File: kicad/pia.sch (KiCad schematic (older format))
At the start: 9 parts, among them J3 DB25_Male, U11 6821, U13 74HC04, U14 74LS245

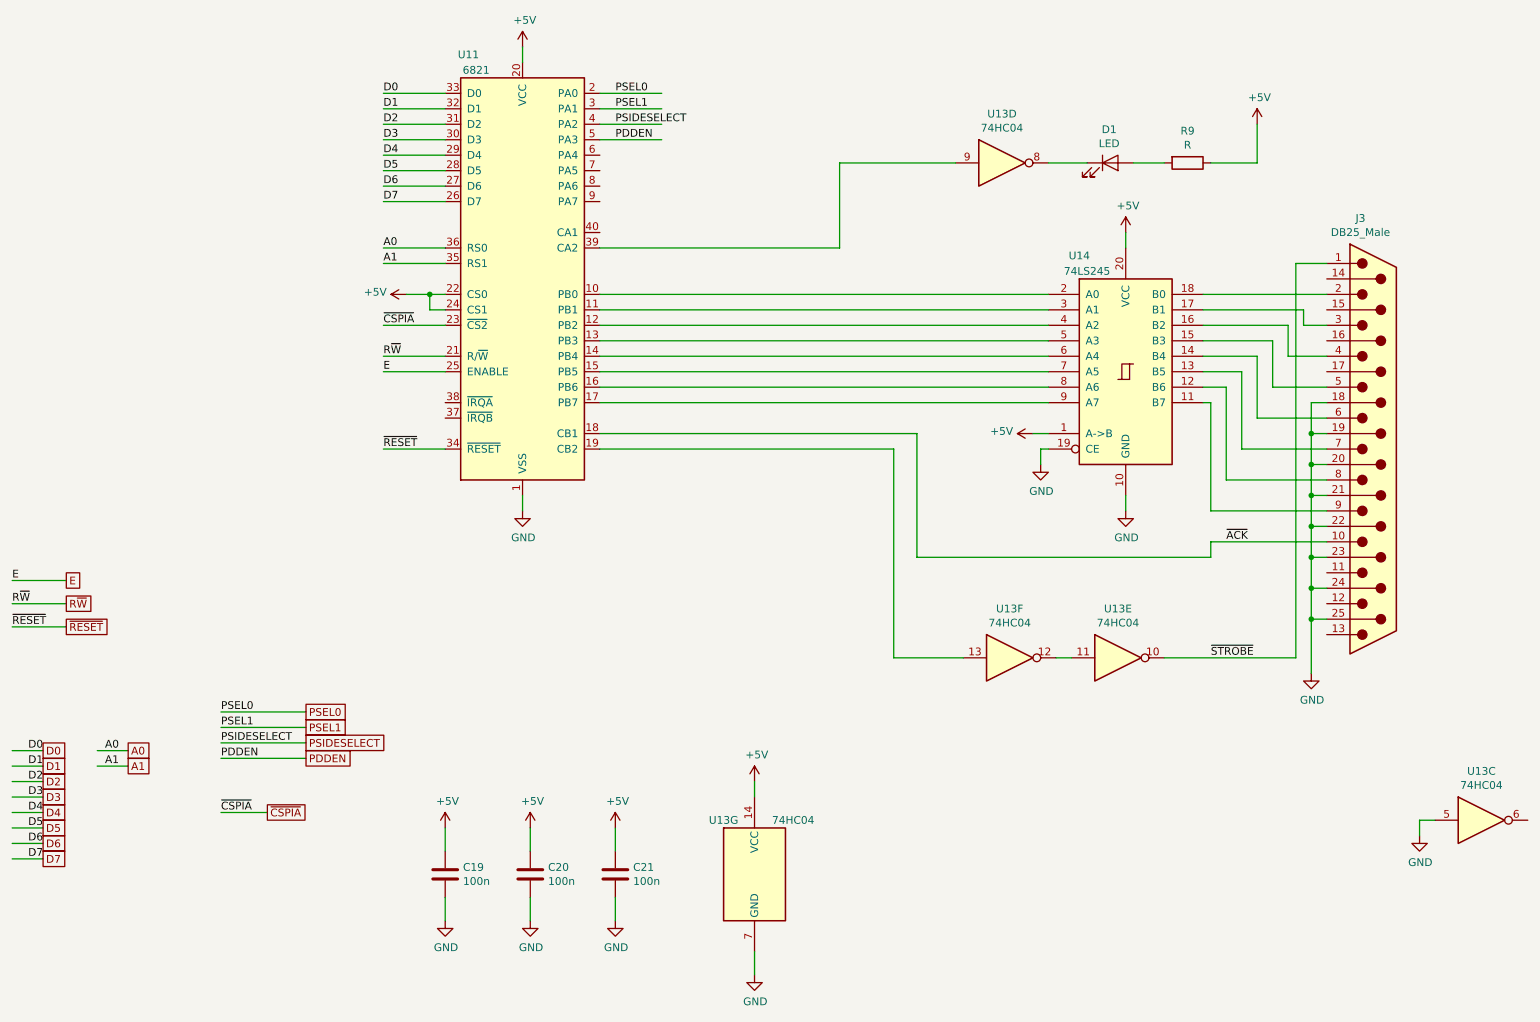
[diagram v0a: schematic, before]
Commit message: Adding PCB layout
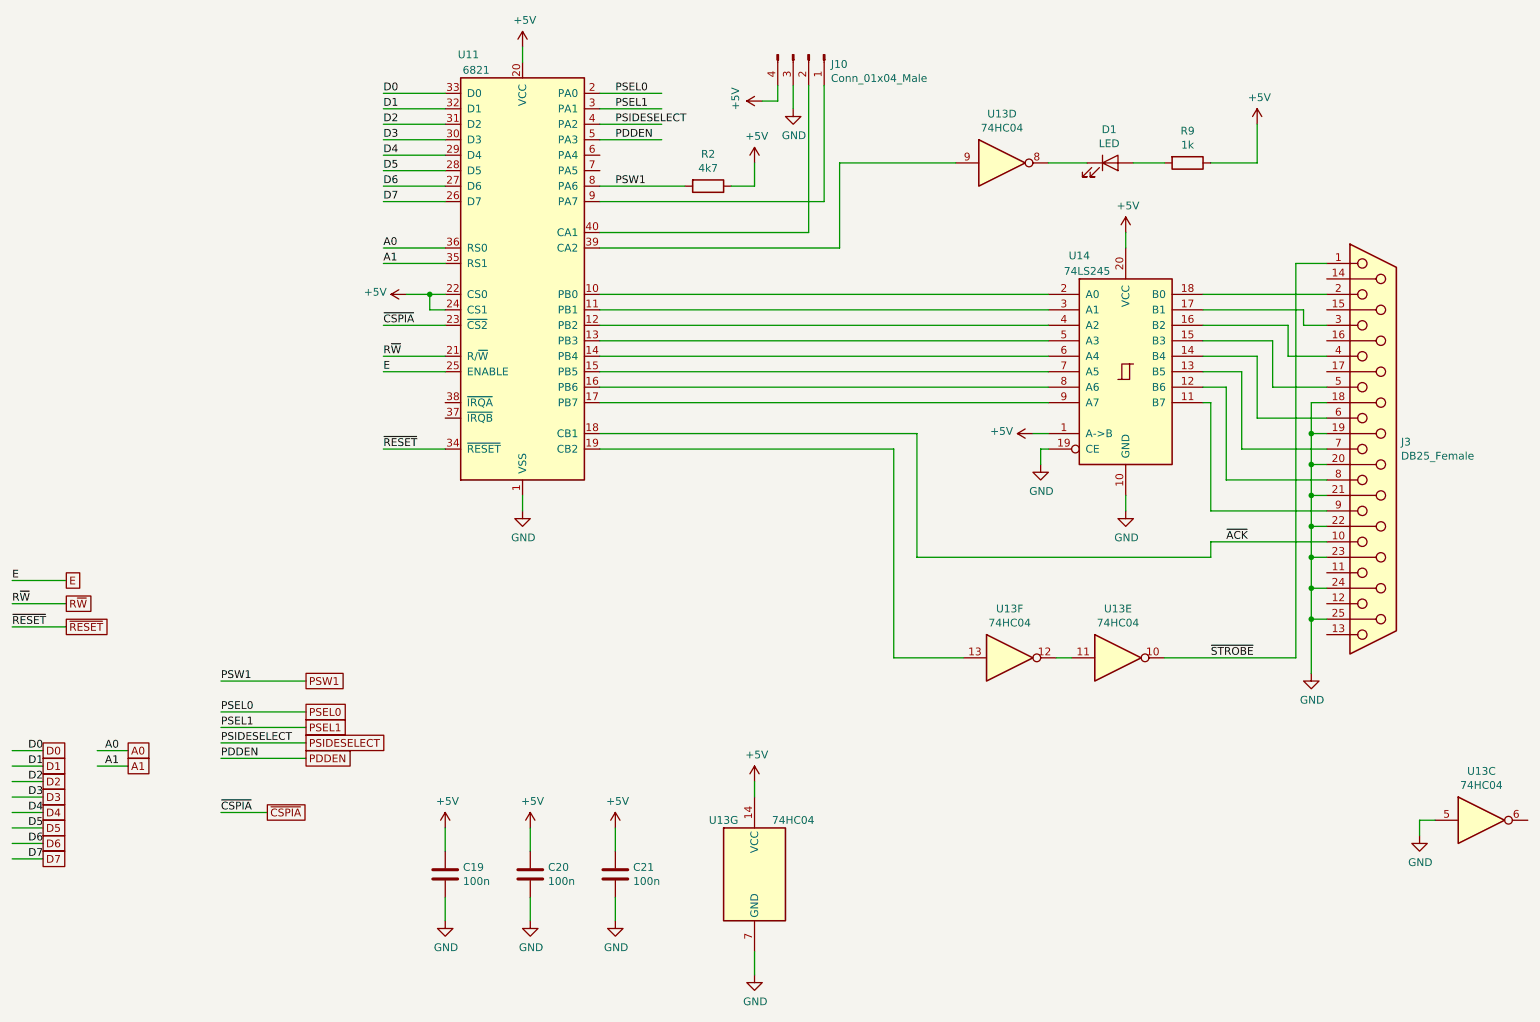
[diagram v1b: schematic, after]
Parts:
- removed J3: DB25_Male, symbol Connector:DB25_Male
- added J10: Conn_01x04_Male, Pin_Headers:Pin_Header_Straight_1x04_Pitch2.54mm, symbol Connector:Conn_01x04_Male
- added J3: DB25_Female, Connectors_DSub:DSUB-25_Female_Horizontal_Pitch2.77x2.84mm_EdgePinOffset7.70mm_Housed_MountingHolesOffset9.12mm, symbol Connector:DB25_Female
- added R2: 4k7, Resistors_THT:R_Axial_DIN0207_L6.3mm_D2.5mm_P7.62mm_Horizontal, symbol Device:R
- D1: footprint (none) -> LEDs:LED_D3.0mm
- R9: value R -> 1k; footprint (none) -> Resistors_THT:R_Axial_DIN0207_L6.3mm_D2.5mm_P7.62mm_Horizontal
- U11: footprint Package_DIP:DIP-40_W15.24mm -> Housings_DIP:DIP-40_W15.24mm_LongPads
- U13: footprint (none) -> Housings_DIP:DIP-14_W7.62mm_LongPads
- U14: footprint (none) -> Housings_DIP:DIP-20_W7.62mm_LongPads
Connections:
- net labels added: PSW1
- wire segments 122 -> 133
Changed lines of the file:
@@
 $Descr A4 11693 8268
 encoding utf-8
-Sheet 5 6
+Sheet 5 7
 Title ""
 Date ""
@@
 F 0 "U11" H 3750 4050 50  0000 C CNN
 F 1 "6821" H 3800 3950 50  0000 C CNN
-F 2 "Package_DIP:DIP-40_W15.24mm" H 4150 1250 50  0001 L CNN
+F 2 "Housings_DIP:DIP-40_W15.24mm_LongPads" H 4150 1250 50  0001 L CNN
 F 3 "http://pdf.datasheetcatalog.com/datasheet/motorola/6821.pdf" H 4100 2600 50  0001 C CNN
 	1    4100 2600
@@
 F 0 "U13" H 7250 5367 50  0000 C CNN
 F 1 "74HC04" H 7250 5276 50  0000 C CNN
-F 2 "" H 7250 5050 50  0001 C CNN
+F 2 "Housings_DIP:DIP-14_W7.62mm_LongPads" H 7250 5050 50  0001 C CNN
 F 3 "http://www.ti.com/lit/gpn/sn74LS04" H 7250 5050 50  0001 C CNN
 	6    7250 5050
@@
 F 0 "U14" H 7700 3950 50  0000 C CNN
 F 1 "74LS245" H 7750 3850 50  0000 C CNN
-F 2 "" H 8000 3200 50  0001 C CNN
+F 2 "Housings_DIP:DIP-20_W7.62mm_LongPads" H 8000 3200 50  0001 C CNN
 F 3 "http://www.ti.com/lit/gpn/sn74LS245" H 8000 3200 50  0001 C CNN
 	1    8000 3200
@@
 F 0 "U13" H 7950 5367 50  0000 C CNN
 F 1 "74HC04" H 7950 5276 50  0000 C CNN
-F 2 "" H 7950 5050 50  0001 C CNN
+F 2 "Housings_DIP:DIP-14_W7.62mm_LongPads" H 7950 5050 50  0001 C CNN
 F 3 "http://www.ti.com/lit/gpn/sn74LS04" H 7950 5050 50  0001 C CNN
 	5    7950 5050
@@
 Wire Wire Line
 	6500 5050 6950 5050
-$Comp
-L Connector:DB25_Male J3
-U 1 1 60EBC120
-P 9600 3700
-F 0 "J3" H 9518 2208 50  0000 C CNN
-F 1 "DB25_Male" H 9518 2299 50  0000 C CNN
-F 2 "" H 9600 3700 50  0001 C CNN
-F 3 " ~" H 9600 3700 50  0001 C CNN
-	1    9600 3700
-	1    0    0    1
-$EndComp
 $Comp
 L power:GND #PWR0173
@@
 F 0 "U13" H 7200 2167 50  0000 C CNN
 F 1 "74HC04" H 7200 2076 50  0000 C CNN
-F 2 "" H 7200 1850 50  0001 C CNN
+F 2 "Housings_DIP:DIP-14_W7.62mm_LongPads" H 7200 1850 50  0001 C CNN
 F 3 "http://www.ti.com/lit/gpn/sn74LS04" H 7200 1850 50  0001 C CNN
 	4    7200 1850
@@
 F 0 "D1" H 7893 2066 50  0000 C CNN
 F 1 "LED" H 7893 1975 50  0000 C CNN
-F 2 "" H 7900 1850 50  0001 C CNN
+F 2 "LEDs:LED_D3.0mm" H 7900 1850 50  0001 C CNN
 F 3 "~" H 7900 1850 50  0001 C CNN
 	1    7900 1850
@@
 P 8400 1850
 F 0 "R9" V 8193 1850 50  0000 C CNN
-F 1 "R" V 8284 1850 50  0000 C CNN
-F 2 "" V 8330 1850 50  0001 C CNN
+F 1 "1k" V 8284 1850 50  0000 C CNN
+F 2 "Resistors_THT:R_Axial_DIN0207_L6.3mm_D2.5mm_P7.62mm_Horizontal" V 8330 1850 50  0001 C CNN
 F 3 "~" H 8400 1850 50  0001 C CNN
 	1    8400 1850
@@
 F 0 "U13" H 10300 6417 50  0000 C CNN
 F 1 "74HC04" H 10300 6326 50  0000 C CNN
-F 2 "" H 10300 6100 50  0001 C CNN
+F 2 "Housings_DIP:DIP-14_W7.62mm_LongPads" H 10300 6100 50  0001 C CNN
 F 3 "http://www.ti.com/lit/gpn/sn74LS04" H 10300 6100 50  0001 C CNN
 	3    10300 6100
@@
 F 0 "U13" H 5400 6800 50  0000 C CNN
 F 1 "74HC04" H 5850 6800 50  0000 C CNN
-F 2 "" H 5600 6450 50  0001 C CNN
+F 2 "Housings_DIP:DIP-14_W7.62mm_LongPads" H 5600 6450 50  0001 C CNN
 F 3 "http://www.ti.com/lit/gpn/sn74LS04" H 5600 6450 50  0001 C CNN
 	7    5600 6450
 	1    0    0    -1
 $EndComp
+$Comp
+L Connector:DB25_Female J3
+U 1 1 611EB53C
+P 9600 3700
+F 0 "J3" H 9780 3746 50  0000 L CNN
+F 1 "DB25_Female" H 9780 3655 50  0000 L CNN
+F 2 "Connectors_DSub:DSUB-25_Female_Horizontal_Pitch2.77x2.84mm_EdgePinOffset7.70mm_Housed_MountingHolesOffset9.12mm" H 9600 3700 50  0001 C CNN
+F 3 " ~" H 9600 3700 50  0001 C CNN
+	1    9600 3700
+	1    0    0    -1
+$EndComp
+Wire Wire Line
+	4600 2000 5150 2000
+$Comp
+L Device:R R2
+U 1 1 61759AE5
+P 5300 2000
+F 0 "R2" V 5093 2000 50  0000 C CNN
+F 1 "4k7" V 5184 2000 50  0000 C CNN
+F 2 "Resistors_THT:R_Axial_DIN0207_L6.3mm_D2.5mm_P7.62mm_Horizontal" V 5230 2000 50  0001 C CNN
+F 3 "~" H 5300 2000 50  0001 C CNN
+	1    5300 2000
+	0    1    1    0
+$EndComp
+Wire Wire Line
+	5450 2000 5600 2000
+Wire Wire Line
+	5600 2000 5600 1850
+$Comp
+L power:+5V #PWR0220
+U 1 1 6175F87F
+P 5600 1850
+F 0 "#PWR0220" H 5600 1700 50  0001 C CNN
+F 1 "+5V" H 5615 2023 50  0000 C CNN
+F 2 "" H 5600 1850 50  0001 C CNN
+F 3 "" H 5600 1850 50  0001 C CNN
+	1    5600 1850
+	1    0    0    -1
+$EndComp
+Text Label 4700 2000 0    50   ~ 0
+PSW1
+Text Label 2150 5200 0    50   ~ 0
+PSW1
+Text GLabel 2700 5200 2    50   UnSpc ~ 0
+PSW1
+Wire Wire Line
+	2700 5200 2150 5200
+Wire Wire Line
+	4600 2300 5950 2300
+$Comp
+L Connector:Conn_01x04_Male J10
+U 1 1 61784020
+P 5950 1150
+F 0 "J10" V 6012 1294 50  0000 L CNN
+F 1 "Conn_01x04_Male" V 6103 1294 50  0000 L CNN
+F 2 "Pin_Headers:Pin_Header_Straight_1x04_Pitch2.54mm" H 5950 1150 50  0001 C CNN
+F 3 "~" H 5950 1150 50  0001 C CNN
+	1    5950 1150
+	0    1    1    0
+$EndComp
+$Comp
+L power:+5V #PWR0221
+U 1 1 6178ADDE
+P 5650 1450
+F 0 "#PWR0221" H 5650 1300 50  0001 C CNN
+F 1 "+5V" H 5665 1623 50  0000 C CNN
+F 2 "" H 5650 1450 50  0001 C CNN
+F 3 "" H 5650 1450 50  0001 C CNN
+	1    5650 1450
+	0    -1   -1   0
+$EndComp
+Wire Wire Line
+	5750 1450 5750 1350
+Wire Wire Line
+	5650 1450 5750 1450
+$Comp
+L power:GND #PWR0222
+U 1 1 6179706B
+P 5850 1500
+F 0 "#PWR0222" H 5850 1250 50  0001 C CNN
+F 1 "GND" H 5855 1327 50  0000 C CNN
+F 2 "" H 5850 1500 50  0001 C CNN
+F 3 "" H 5850 1500 50  0001 C CNN
+	1    5850 1500
+	1    0    0    -1
+$EndComp
+Wire Wire Line
+	5850 1350 5850 1500
+Wire Wire Line
+	6050 2100 6050 1350
+Wire Wire Line
+	4600 2100 6050 2100
+Wire Wire Line
+	5950 1350 5950 2300
 $EndSCHEMATC

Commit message: Adding PCB
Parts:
- removed J10: Conn_01x04_Male, Pin_Headers:Pin_Header_Straight_1x04_Pitch2.54mm, symbol Connector:Conn_01x04_Male
- added J10: Conn_01x06_Male, Pin_Headers:Pin_Header_Straight_1x06_Pitch2.54mm, symbol Connector:Conn_01x06_Male
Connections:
- wire segments 133 -> 136
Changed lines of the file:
@@
 	1    0    0    -1
 $EndComp
-Wire Wire Line
-	6150 1850 6900 1850
 $Comp
 L Device:LED D1
@@
 Text Label 4700 1700 0    50   ~ 0
 PDDEN
-Wire Wire Line
-	4600 2400 6150 2400
-Wire Wire Line
-	6150 2400 6150 1850
 Text GLabel 1000 5650 2    50   UnSpc ~ 0
 D0
@@
 U 1 1 61759AE5
 P 5300 2000
-F 0 "R2" V 5093 2000 50  0000 C CNN
-F 1 "4k7" V 5184 2000 50  0000 C CNN
+F 0 "R2" V 5450 1900 50  0000 C CNN
+F 1 "4k7" V 5450 2100 50  0000 C CNN
 F 2 "Resistors_THT:R_Axial_DIN0207_L6.3mm_D2.5mm_P7.62mm_Horizontal" V 5230 2000 50  0001 C CNN
 F 3 "~" H 5300 2000 50  0001 C CNN
@@
 Wire Wire Line
 	5450 2000 5600 2000
-Wire Wire Line
-	5600 2000 5600 1850
 $Comp
 L power:+5V #PWR0220
 U 1 1 6175F87F
-P 5600 1850
-F 0 "#PWR0220" H 5600 1700 50  0001 C CNN
-F 1 "+5V" H 5615 2023 50  0000 C CNN
-F 2 "" H 5600 1850 50  0001 C CNN
-F 3 "" H 5600 1850 50  0001 C CNN
-	1    5600 1850
-	1    0    0    -1
+P 5600 2000
+F 0 "#PWR0220" H 5600 1850 50  0001 C CNN
+F 1 "+5V" H 5615 2173 50  0000 C CNN
+F 2 "" H 5600 2000 50  0001 C CNN
+F 3 "" H 5600 2000 50  0001 C CNN
+	1    5600 2000
+	0    1    1    0
 $EndComp
 Text Label 4700 2000 0    50   ~ 0
@@
 Wire Wire Line
 	4600 2300 5950 2300
-$Comp
-L Connector:Conn_01x04_Male J10
-U 1 1 61784020
-P 5950 1150
-F 0 "J10" V 6012 1294 50  0000 L CNN
-F 1 "Conn_01x04_Male" V 6103 1294 50  0000 L CNN
-F 2 "Pin_Headers:Pin_Header_Straight_1x04_Pitch2.54mm" H 5950 1150 50  0001 C CNN
-F 3 "~" H 5950 1150 50  0001 C CNN
-	1    5950 1150
-	0    1    1    0
-$EndComp
 $Comp
 L power:+5V #PWR0221
@@
 Wire Wire Line
 	5950 1350 5950 2300
+Wire Wire Line
+	6700 2400 6700 1850
+Wire Wire Line
+	6700 1850 6900 1850
+Wire Wire Line
+	4600 2400 6700 2400
+$Comp
+L Connector:Conn_01x06_Male J10
+U 1 1 61867758
+P 5950 1150
+F 0 "J10" V 6012 762 50  0000 R CNN
+F 1 "Conn_01x06_Male" V 6103 762 50  0000 R CNN
+F 2 "Pin_Headers:Pin_Header_Straight_1x06_Pitch2.54mm" H 5950 1150 50  0001 C CNN
+F 3 "~" H 5950 1150 50  0001 C CNN
+	1    5950 1150
+	0    -1   1    0
+$EndComp
+Wire Wire Line
+	4600 1800 6150 1800
+Wire Wire Line
+	6150 1800 6150 1350
+Wire Wire Line
+	6250 1900 6250 1350
+Wire Wire Line
+	4600 1900 6250 1900
 $EndSCHEMATC
